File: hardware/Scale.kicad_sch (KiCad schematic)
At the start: 3 parts, among them J1 Load Cell Connector, J4 GPIO, J5 RS232

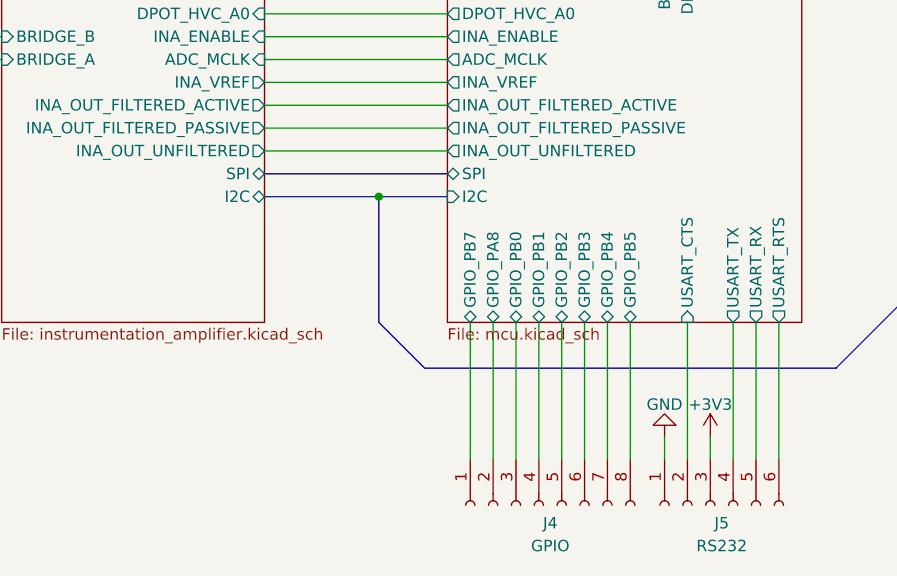
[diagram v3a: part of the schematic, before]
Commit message: Regenerated reference designators, changed to rail-to-rail op-amps
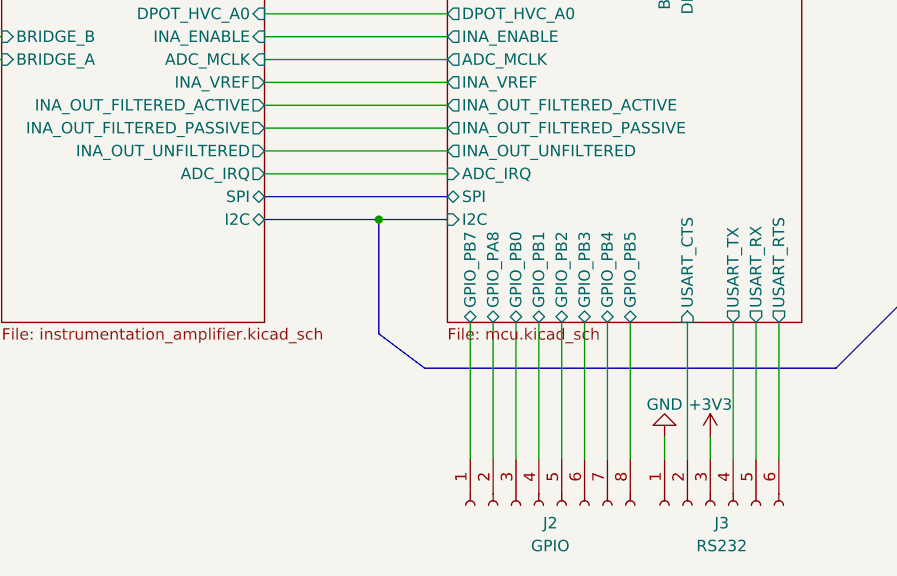
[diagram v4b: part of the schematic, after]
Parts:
- renumbered J4 to J2, J5 to J3
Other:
- sheet Instrumentation Amplifier ports: added ADC_IRQ; removed none
- sheet MCU ports: added ADC_IRQ; removed none

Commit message: Started on pcb
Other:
- added sheet ADC (adc.kicad_sch)
- sheet Display ports: added {I2C}; removed I2C
- sheet Instrumentation Amplifier ports: added ADC_VREF, INA_IN_N, INA_IN_P, {I2C}; removed ADC_IRQ, ADC_MCLK, I2C, INA_VREF, SPI
- sheet MCU ports: added I2C1{I2C}, SPI2{SPI}; removed I2C, SPI

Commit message: Some more routing
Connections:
- net MCU/GPIO_PA8 renamed MCU/GPIO_PB6
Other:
- sheet MCU ports: added GPIO_PB6; removed GPIO_PA8, LDO_EN
- sheet Power ports: added none; removed LDO_EN
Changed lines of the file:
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@@
-	(wire
-		(pts
-			(xy 139.7 68.58) (xy 139.7 80.01)
-		)
-		(stroke
-			(width 0)
-			(type default)
-		)
-	)
 	(wire
 		(pts
@@
 			)
 		)
-		(pin "LDO_EN" input
-			(at 139.7 68.58 270)
-			(effects
-				(font
-					(size 1.27 1.27)
-				)
-				(justify left)
-			)
-		)
 		(instances
 			(project "Scale"
@@
 			)
 		)
-		(pin "GPIO_PA8" bidirectional
-			(at 124.46 130.81 270)
-			(effects
-				(font
-					(size 1.27 1.27)
-				)
-				(justify left)
-			)
-		)
 		(pin "SPI2{SPI}" bidirectional
 			(at 119.38 119.38 180)
@@
 			)
 		)
-		(pin "LDO_EN" output
-			(at 139.7 80.01 90)
-			(effects
-				(font
-					(size 1.27 1.27)
-				)
-				(justify right)
-			)
-		)
 		(pin "I2C1{I2C}" bidirectional
 			(at 119.38 116.84 180)
@@
 			(effects
 				(font
+					(size 1.27 1.27)
+				)
+				(justify left)
+			)
+		)
+		(pin "GPIO_PB6" bidirectional
+			(at 124.46 130.81 270)
+			(effects
+				(font

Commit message: Ran electrical check on schematic and implemented corrections
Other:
- sheet ADC ports: added INA_OUT_FILTERED_PASSIVE; removed none
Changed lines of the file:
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@@
+	)
+	(junction
+		(at 105.41 109.22)
+		(diameter 0)
+		(color 0 0 0 0)
 	)
 	(junction
@@
 	(wire
 		(pts
+			(xy 105.41 109.22) (xy 119.38 109.22)
+		)
+		(stroke
+			(width 0)
+			(type default)
+		)
+	)
+	(wire
+		(pts
+			(xy 83.82 142.24) (xy 83.82 139.7)
+		)
+		(stroke
+			(width 0)
+			(type default)
+		)
+	)
+	(wire
+		(pts
 			(xy 76.2 130.81) (xy 76.2 142.24)
 		)
@@
 	(wire
 		(pts
+			(xy 83.82 139.7) (xy 105.41 139.7)
+		)
+		(stroke
+			(width 0)
+			(type default)
+		)
+	)
+	(wire
+		(pts
 			(xy 78.74 137.16) (xy 102.87 137.16)
 		)
@@
 	(wire
 		(pts
-			(xy 99.06 109.22) (xy 119.38 109.22)
+			(xy 99.06 109.22) (xy 105.41 109.22)
 		)
 		(stroke
@@
 		(pts
 			(xy 99.06 82.55) (xy 119.38 82.55)
+		)
+		(stroke
+			(width 0)
+			(type default)
+		)
+	)
+	(wire
+		(pts
+			(xy 105.41 109.22) (xy 105.41 139.7)
 		)
 		(stroke
@@
 			(effects
 				(font
+					(size 1.27 1.27)
+				)
+				(justify right)
+			)
+		)
+		(pin "INA_OUT_FILTERED_PASSIVE" output
+			(at 83.82 142.24 90)
+			(effects
+				(font
